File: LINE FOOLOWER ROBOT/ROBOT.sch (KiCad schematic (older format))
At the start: 81 parts

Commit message: shema
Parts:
- removed +5V? (x3): +5V, symbol +5V
- removed 9V? (x2): 9V, symbol 9V
- removed GND?: GND, symbol GND
- removed NPN?: Q1, FOOTPRINT:KSP2222A, symbol Q1
- removed R150? (x2): R, symbol R
- removed RESISTOR?: 2K, symbol 2K
- added 100R: 1R, symbol 100R
- added 100R: 2R, symbol 100R
- added 100R: 3R, symbol 100R
- added 100R: 4R, symbol 100R
- added 100R: 5R, symbol 100R
- added 100R: 6R, symbol 100R
- added 100R: 7R, symbol 100R
- added 100R: 8R, symbol 100R
- added 100R: 9R, symbol 100R
- added 100R? (x5): 100R, symbol 100R
- added 5V? (x5): 5VARD, symbol 5VARD
- added GND (x7), GND? (x6): GND, symbol GND
- added NPN: Q1, FOOTPRINT:KSP2222A, symbol Q1
- added NPN: Q2, FOOTPRINT:KSP2222A, symbol Q1
- added U? (x4): 5VREG, symbol 5VREG
- SFH4550: renamed from SFH4550?; value SFH4550 -> Q1
- SFH4550: renamed from SFH4550?; value SFH4550 -> D4
- SFH4550?: value SFH4550 -> Q3
- SFH4550?: value SFH4550 -> Q2
- gave numbers to parts that had none: 9
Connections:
- net labels added: D5, DS1, DS2, DS3, DS4, MUX, S0, S1, S2
- wire segments 56 -> 179
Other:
- moved on the sheet: +5V?, BPW85B, BPW85B?, ENCODER?, GND, GND?, MUX4051, NPN?, QRE1113?, RES, RES1, RES2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

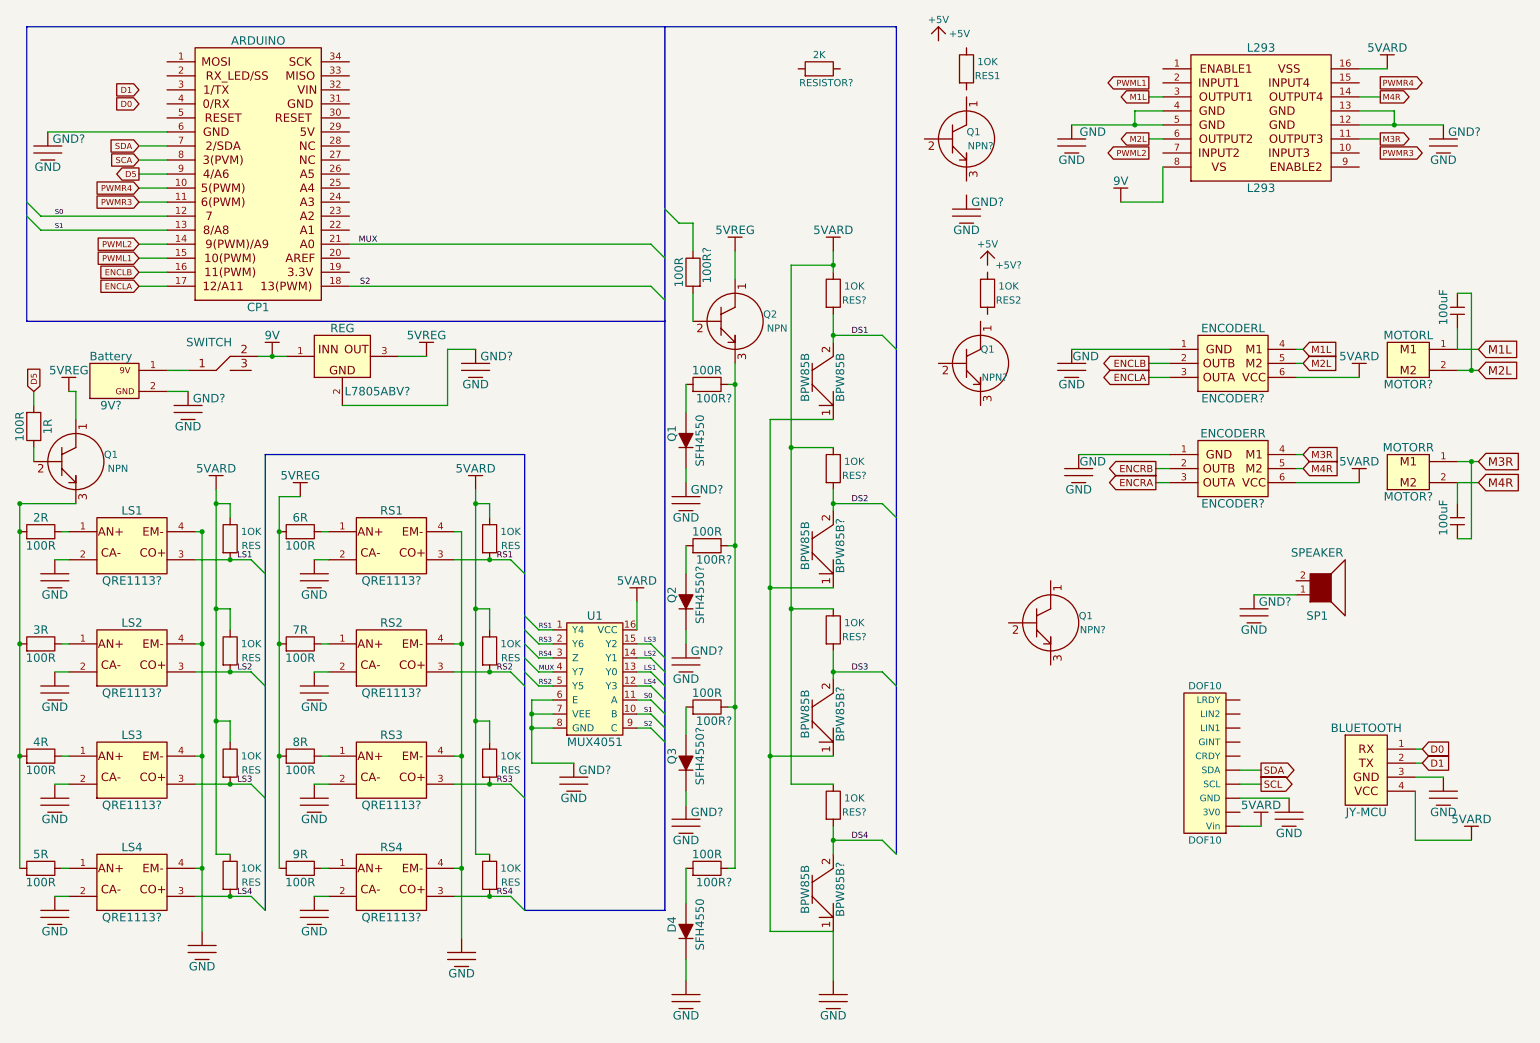
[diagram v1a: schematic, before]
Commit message: SHEMA FINALL
Vključeni so tudi senzorji za odboj svetlobe, glede na to da bomo vozili
samo po črti jih lahko tudi izločim iz sheme. Bo več prostih pinov na
mikro krmilniku.
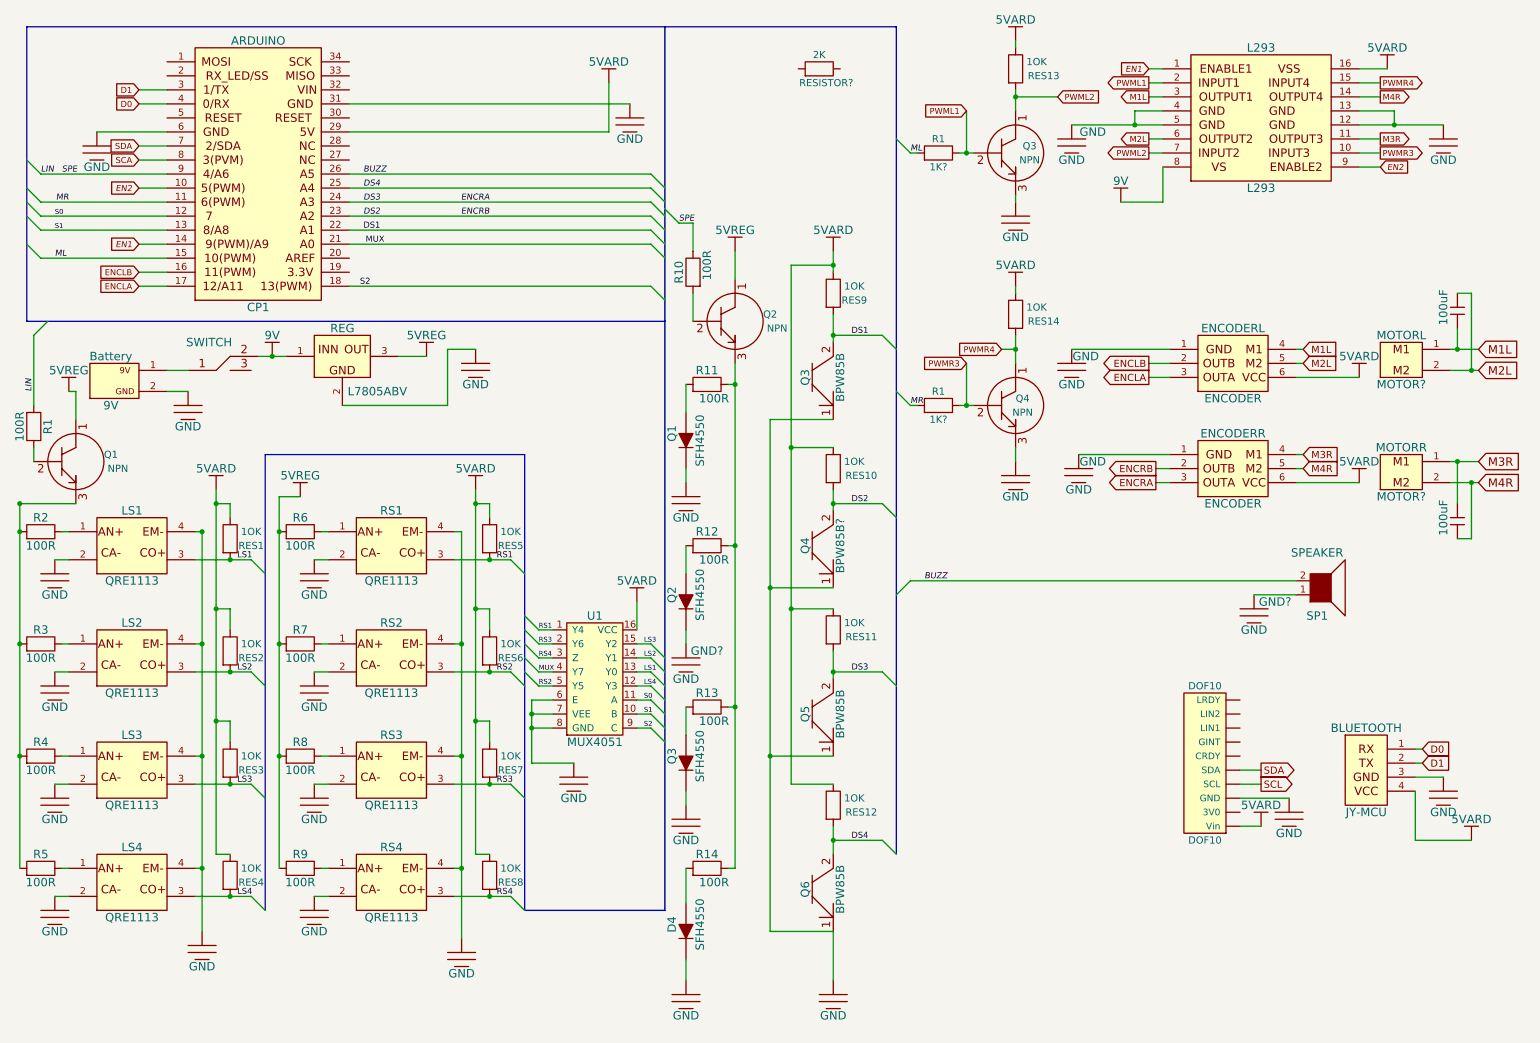
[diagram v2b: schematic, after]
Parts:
- removed +5V, +5V?: +5V, symbol +5V
- removed NPN?: Q1, symbol Q1
- added 1K? (x2): R1, symbol R1
- added 5V? (x3): 5VARD, symbol 5VARD
- added GND, GND?: GND, symbol GND
- 100R: value 1R -> R1
- 100R: value 2R -> R2
- 100R: value 3R -> R3
- 100R: value 4R -> R4
- 100R: value 5R -> R5
- 100R: value 6R -> R6
- 100R: value 7R -> R7
- 100R: value 8R -> R8
- 100R: value 9R -> R9
- 100R: renamed from 100R?; value 100R -> R10
- 100R: renamed from 100R?; value 100R -> R11
- 100R: renamed from 100R?; value 100R -> R12
- 100R: renamed from 100R?; value 100R -> R13
- 100R: renamed from 100R?; value 100R -> R14
- BPW85B: renamed from BPW85B?; value BPW85B -> Q5
- BPW85B: renamed from BPW85B?; value BPW85B -> Q6
- BPW85B: value BPW85B -> Q3
- BPW85B?: value BPW85B -> Q4
- NPN: renamed from NPN?; value Q1 -> Q3
- NPN: renamed from NPN?; value Q1 -> Q4
- gave numbers to parts that had none: 10
- renumbered RES to RES1, RES1 to RES13, RES2 to RES14, RES to RES2, RES to RES3, RES to RES4, RES to RES5, RES to RES6, RES to RES7, RES to RES8
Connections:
- net D5 is gone; now on net LIN: 100R.~, CP1.9
- net DS2 is gone; now on net ENCRB: BPW85B?.~, RES10.~
- net DS3 is gone; now on net ENCRA: BPW85B.~, RES11.~
- net D0: now also CP1.4
- net D1: now also CP1.3
- net DS1: now also CP1.22
- net DS4: now also CP1.25
- net ENCRA: now also CP1.24
- net ENCRB: now also CP1.23
- net PWML1: now also L293.2, NPN.~, 1K?.~; no longer CP1.15
- net PWML2: now also L293.7, NPN.~, RES13.~; no longer CP1.14
- net PWMR3: now also L293.10, NPN.~, 1K?.~; no longer CP1.11
- net PWMR4: now also L293.15, NPN.~, RES14.~; no longer CP1.10
- net BUZZ: now reaches CP1.26
- net BUZZ: now also SP1.2
- net at CP1.29: now also 5V?.~
- net at CP1.31: now also GND.~
- net EN1: now reaches L293.1
- net EN1: now also CP1.14
- net EN2: now reaches L293.9
- net EN2: now also CP1.10
- net at GND?.~: now also NPN.~
- net at SFH4550.~: now also GND?.~; no longer 100R.~ (x4)
- net at NPN.~: now also 100R.~, 100R.~, 100R.~, 100R.~; no longer 100R.~ (x2)
- net LIN: now reaches 100R.~
- new net: 5V?.~, RES14.~
- new net: 5V?.~, RES13.~
- new net: GND?.~, NPN.~
- new net: BPW85B.~, BPW85B.~, BPW85B.~, BPW85B?.~, GND?.~
- new net: 100R.~, SFH4550.~ (x4)
- new net: 5V?.~, RES10.~, RES11.~, RES12.~, RES9.~
- new net: 5V?.~, RES1.~, RES2.~, RES3.~, RES4.~
- new net: 5V?.~, RES5.~, RES6.~, RES7.~, RES8.~
- new net: 100R.~, NPN.~ (x2)
- new net ML: 1K?.~, CP1.15
- new net MR: 1K?.~, CP1.11
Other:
- moved on the sheet: MOTOR?, NPN, RES13, RES14

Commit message: Na pol poti....
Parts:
- removed 100R: R10, symbol 100R
- removed 100R: R11, symbol 100R
- removed 100R: R12, symbol 100R
- removed 100R: R13, symbol 100R
- removed 100R: R14, symbol 100R
- removed 1K? (x2): R1, symbol R1
- removed 5V? (x3): 5VARD, symbol 5VARD
- removed BPW85B: Q5, symbol BPW85B
- removed BPW85B: Q6, symbol BPW85B
- removed BPW85B: Q3, symbol BPW85B
- removed BPW85B?: Q4, symbol BPW85B
- removed GND? (x7): GND, symbol GND
- removed NPN: Q3, symbol Q1
- removed NPN: Q4, symbol Q1
- removed NPN: Q2, FOOTPRINT:KSP2222A, symbol Q1
- removed RES10, RES11, RES12, RES13, RES14, RES9: 1OK, symbol 1OK
- removed RESISTOR?: 2K, symbol 2K
- removed SFH4550: Q3, symbol SFH4550
- removed SFH4550: Q1, symbol SFH4550
- removed SFH4550: Q2, symbol SFH4550
- removed SFH4550: D4, symbol SFH4550
- removed U?: 5VREG, symbol 5VREG
- added 5V? (x3): 5VARD, symbol 5VARD
- added GND?: GND, symbol GND
- added RES?: 1OK, symbol 1OK
- added U?: PUSH_B., symbol PUSH_B.
- 100R3: renamed from 100R; footprint (none) -> K
- 9V1: renamed from 9V; footprint (none) -> FOOTPRINT:9V_BATTERY_HOLDER
- CP1: footprint (none) -> FOOTPRINT:ARDUINO_MICRO_SHIELD
- L7805ABV1: renamed from L7805ABV; footprint (none) -> FOOTPRINT:REGULATOR
- RES1: footprint (none) -> FOOTPRINT:RESISTOR
- gave numbers to parts that had none: 25
- renumbered 100R to 100R1, 100R to 100R2, 100R to 100R4, 100R to 100R5, 100R to 100R6, 100R to 100R7, 100R to 100R8, 100R to 100R9, 9V to 9V2, 9V to 9V3, ENCODER to ENCODER1, ENCODER to ENCODER2, GND to GND1, GND to GND10, GND to GND11, GND to GND15, GND to GND2, GND to GND23, GND to GND24, GND to GND25, GND to GND28, GND to GND3, GND to GND4, GND to GND5, GND to GND8, GND to GND9, JY-MCU to JY-MCU1, NPN to NPN1, QRE1113 to QRE1113-1, QRE1113 to QRE1113-2, QRE1113 to QRE1113-3, QRE1113 to QRE1113-4, QRE1113 to QRE1113-5, QRE1113 to QRE1113-6, QRE1113 to QRE1113-7, QRE1113 to QRE1113-8
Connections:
- net ML is gone; now on net PWML2: CP1.15
- net MR is gone; now on net PWMR4: CP1.11
- net PWML1: now also CP1.14
- net PWMR3: now also CP1.10
- net at NPN1.~: now also 100R2.~, 100R3.~, 100R4.~, 100R5.~; no longer 100R1.~
- net DS1: no longer names the net of CP1.22
- net DS4 renamed BUT
- net BUT: now also RES?.~, U?.~
- net EN1: no longer names the net of L293.1
- net EN1: now also 5V?.~; no longer CP1.14
- net EN2: no longer names the net of L293.9
- net EN2: now also 5V?.~; no longer CP1.10
- new net: 5V1.~, RES1.~, RES2.~, RES3.~, RES4.~
- new net: 5V2.~, RES5.~, RES6.~, RES7.~, RES8.~
- new net: 100R1.~, NPN1.~
- new net: 5V?.~, RES?.~
- new net: GND?.~, U?.~
